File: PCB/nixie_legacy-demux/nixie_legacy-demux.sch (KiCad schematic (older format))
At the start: 38 parts, among them J1 HEADER_3, J2 K155ID1, Q1 MPSA42, Q2 MPSA42, Q3 MPSA42, Q4 MPSA42, Q5 MPSA42, Q6 MPSA42, U1 ATMEGA328P-PU, U2 MC7805CT-BP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

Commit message: added i2c_rtc_test.c to test interfacing with RX8025 rtc module
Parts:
- added J4: RX-8025SA, Package_SO:SOP-16_4.4x10.4mm_P1.27mm, symbol w_connectors:HEADER_14
- added R20, R21: 3.3k, Resistor_THT:R_Axial_DIN0207_L6.3mm_D2.5mm_P7.62mm_Horizontal, symbol Device:R_US
- gave numbers to parts that had none: 4
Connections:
- wire segments 175 -> 201
- no-connect marks 13 -> 22
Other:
- note added: "should I add a backup battery???"
- note removed: "If we add a clock module,\nthis is where it can go.\n\nIt will need to slot into the control board \nusing some sort of breakout header, probably. \n\nCommunication is over I2C, I think."

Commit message: Demux circuit schematic now complete with RTC (including 1Hz interrupt pin)
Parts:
- removed C1: 220nTANT, Capacitor_THT:C_Disc_D3.8mm_W2.6mm_P2.50mm, symbol Device:CP1
- removed SW1: Select_butt, symbol Switch:SW_Push
- removed SW2: Up_butt, symbol Switch:SW_Push
- removed SW3: Down_butt, symbol Switch:SW_Push
- removed U2: MC7805CT-BP, digikey-footprints:TO-220-3, symbol dk_PMIC-Voltage-Regulators-Linear:MC7805CT-BP
- added J5: HEADER_4, Connector_PinHeader_2.54mm:PinHeader_1x04_P2.54mm_Vertical, symbol w_connectors:HEADER_4
- J3: footprint (none) -> Connector_PinHeader_2.54mm:PinHeader_2x09_P2.54mm_Vertical
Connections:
- net labels removed: 9v
- wire segments 201 -> 194
- no-connect marks 22 -> 19
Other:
- note added: "down\nup\nselect\nGND"
- note removed: "should I add a backup battery???"
- moved on the sheet: J4, R20, R21

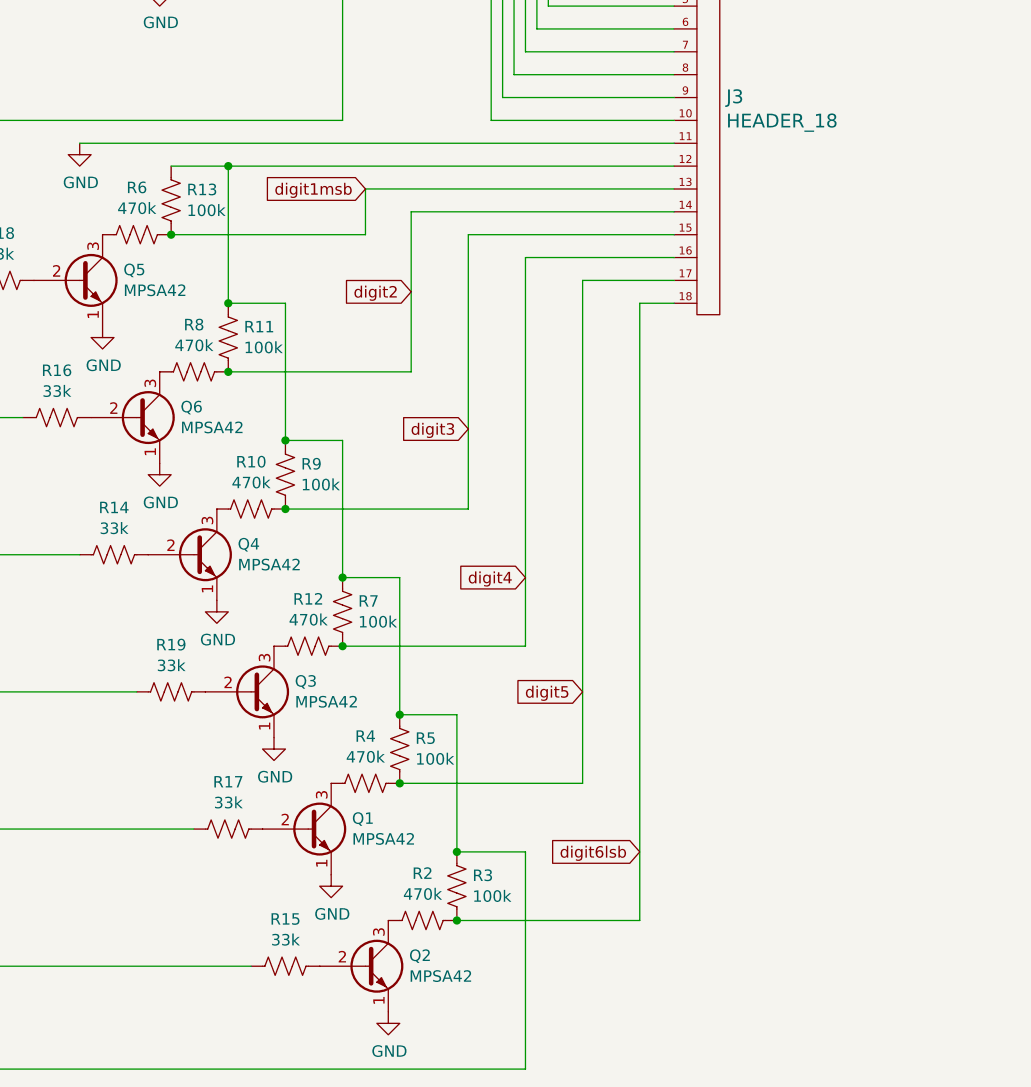
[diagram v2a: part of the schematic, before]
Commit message: Adding demux PCB v1: uses resistor network for 100k, has npn on board but pnp is on digit board
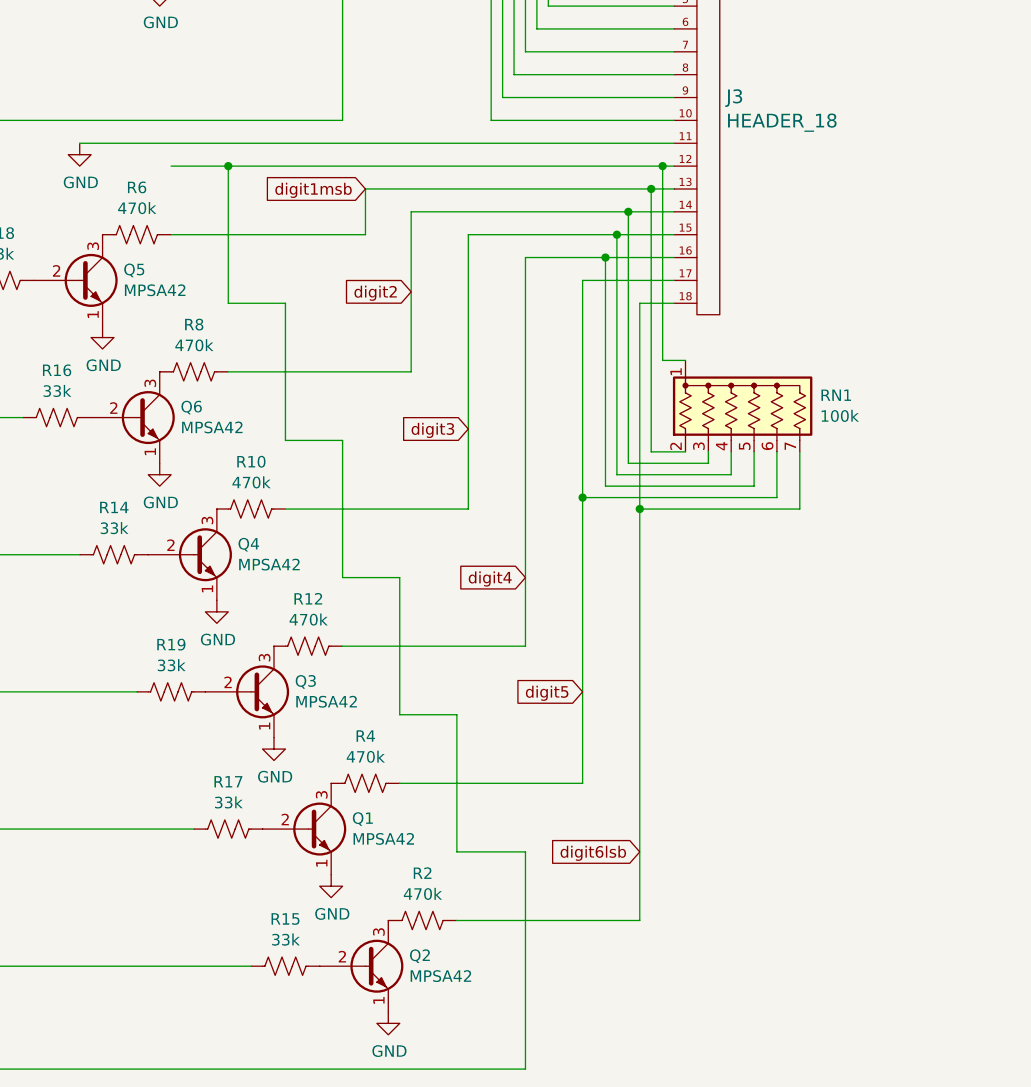
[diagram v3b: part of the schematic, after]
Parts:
- removed R11, R13, R3, R5, R7, R9: 100k, Resistor_THT:R_Axial_DIN0207_L6.3mm_D2.5mm_P7.62mm_Horizontal, symbol Device:R_US
- added RN1: 100k, Resistor_THT:R_Array_SIP7, symbol Device:R_Network06_US
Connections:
- net 200v: now also RN1.1 (common)
- net digit1msb: now also RN1.2 (R1)
- net digit2: now also RN1.3 (R2)
- net digit3: now also RN1.4 (R3)
- net digit4: now also RN1.5 (R4)
- net digit5: now also RN1.6 (R5)
- net digit6lsb: now also RN1.7 (R6)
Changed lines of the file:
@@
-$EndComp
-$Comp
-L Device:R_US R3
-U 1 1 60FDEAA9
-P 5900 6850
-F 0 "R3" H 5968 6896 50  0000 L CNN
-F 1 "100k" H 5968 6805 50  0000 L CNN
-F 2 "Resistor_THT:R_Axial_DIN0207_L6.3mm_D2.5mm_P7.62mm_Horizontal" V 5940 6840 50  0001 C CNN
-F 3 "~" H 5900 6850 50  0001 C CNN
-	1    5900 6850
-	1    0    0    -1
-$EndComp
-$Comp
-L Device:R_US R5
-U 1 1 60FDEAB3
-P 5650 6250
-F 0 "R5" H 5718 6296 50  0000 L CNN
-F 1 "100k" H 5718 6205 50  0000 L CNN
-F 2 "Resistor_THT:R_Axial_DIN0207_L6.3mm_D2.5mm_P7.62mm_Horizontal" V 5690 6240 50  0001 C CNN
-F 3 "~" H 5650 6250 50  0001 C CNN
-	1    5650 6250
-	1    0    0    -1
-$EndComp
-$Comp
-L Device:R_US R7
-U 1 1 60FDEABD
-P 5400 5650
-F 0 "R7" H 5468 5696 50  0000 L CNN
-F 1 "100k" H 5468 5605 50  0000 L CNN
-F 2 "Resistor_THT:R_Axial_DIN0207_L6.3mm_D2.5mm_P7.62mm_Horizontal" V 5440 5640 50  0001 C CNN
-F 3 "~" H 5400 5650 50  0001 C CNN
-	1    5400 5650
-	1    0    0    -1
-$EndComp
-$Comp
-L Device:R_US R9
-U 1 1 60FDEAC7
-P 5150 5050
-F 0 "R9" H 5218 5096 50  0000 L CNN
-F 1 "100k" H 5218 5005 50  0000 L CNN
-F 2 "Resistor_THT:R_Axial_DIN0207_L6.3mm_D2.5mm_P7.62mm_Horizontal" V 5190 5040 50  0001 C CNN
-F 3 "~" H 5150 5050 50  0001 C CNN
-	1    5150 5050
-	1    0    0    -1
-$EndComp
-$Comp
-L Device:R_US R11
-U 1 1 60FDEAD1
-P 4900 4450
-F 0 "R11" H 4968 4496 50  0000 L CNN
-F 1 "100k" H 4968 4405 50  0000 L CNN
-F 2 "Resistor_THT:R_Axial_DIN0207_L6.3mm_D2.5mm_P7.62mm_Horizontal" V 4940 4440 50  0001 C CNN
-F 3 "~" H 4900 4450 50  0001 C CNN
-	1    4900 4450
-	1    0    0    -1
 $EndComp
 $Comp
@@
 Wire Wire Line
 	5650 5500 5400 5500
-Connection ~ 5650 6100
 Wire Wire Line
 	5400 5500 5400 4900
 Wire Wire Line
 	5400 4900 5150 4900
-Connection ~ 5400 5500
 Wire Wire Line
 	5150 4900 5150 4300
 Wire Wire Line
 	5150 4300 4900 4300
-Connection ~ 5150 4900
 Wire Wire Line
 	4900 4300 4900 3700
 Wire Wire Line
 	4900 3700 4650 3700
-Connection ~ 4900 4300
 Wire Wire Line
 	1450 1150 1300 1150
@@
 Text GLabel 5950 4850 0    50   Input ~ 0
 digit3
-Connection ~ 5150 5200
-Connection ~ 5400 5800
-Connection ~ 5650 6400
-Connection ~ 5900 7000
-Connection ~ 4900 4600
 Text GLabel 5700 4250 0    50   Input ~ 0
 digit2
@@
 Wire Wire Line
 	1450 1700 1450 1150
-Connection ~ 5900 6700
 Wire Wire Line
 	2050 3800 3400 3800
@@
 	6850 4200 6450 4200
 Wire Wire Line
-	6850 4100 6200 4100
+	6850 4100 6550 4100
 Wire Wire Line
 	6200 4100 6200 5800
@@
 	5950 4000 5950 5200
 Wire Wire Line
-	6850 3900 5700 3900
-Wire Wire Line
 	5700 3900 5700 4600
 Wire Wire Line
 	5500 4000 5500 3800
 Wire Wire Line
-	5500 3800 6850 3800
+	5500 3800 6750 3800
 Wire Wire Line
 	4900 4600 5700 4600
@@
 $EndComp
 Wire Wire Line
-	6850 3700 4900 3700
+	6850 3700 6800 3700
 Connection ~ 4900 3700
 Wire Wire Line
@@
 	6850 3400 6100 3400
 Wire Wire Line
-	5950 4000 6850 4000
-Wire Wire Line
-	6450 4200 6450 6400
-Wire Wire Line
-	6700 4300 6700 7000
+	5950 4000 6600 4000
+Wire Wire Line
+	6450 4200 6450 5150
+Wire Wire Line
+	6700 4300 6700 5200
 Wire Wire Line
 	5400 750  5400 950
@@
 Wire Wire Line
 	4650 4000 5500 4000
-Connection ~ 4650 4000
-$Comp
-L Device:R_US R13
-U 1 1 60FDEADB
-P 4650 3850
-F 0 "R13" H 4718 3896 50  0000 L CNN
-F 1 "100k" H 4718 3805 50  0000 L CNN
-F 2 "Resistor_THT:R_Axial_DIN0207_L6.3mm_D2.5mm_P7.62mm_Horizontal" V 4690 3840 50  0001 C CNN
-F 3 "~" H 4650 3850 50  0001 C CNN
-	1    4650 3850
-	1    0    0    -1
-$EndComp
 $Comp
 L Device:R_US R6
@@
 Wire Wire Line
 	1000 950  2650 950
+Wire Wire Line
+	6800 4550 6800 3700
+Connection ~ 6800 3700
+Wire Wire Line
+	6800 3700 4900 3700
+Wire Wire Line
+	6750 4950 6750 3800
+Connection ~ 6750 3800
+Wire Wire Line
+	6750 3800 6850 3800
+Wire Wire Line
+	6850 3900 6650 3900
+Wire Wire Line
+	7000 4950 7000 5000
+Wire Wire Line
+	6650 5000 6650 3900
+Connection ~ 6650 3900
+Wire Wire Line
+	6650 3900 5700 3900
+Wire Wire Line
+	7100 4950 7100 5050
+Wire Wire Line
+	6600 5050 6600 4000
+Connection ~ 6600 4000
+Wire Wire Line
+	6600 4000 6850 4000
+Wire Wire Line
+	7200 4950 7200 5100
+Wire Wire Line
+	6550 5100 6550 4100
+Connection ~ 6550 4100
+Wire Wire Line
+	6550 4100 6200 4100
+Wire Wire Line
+	7300 4950 7300 5150
+Connection ~ 6450 5150
+Wire Wire Line
+	6450 5150 6450 6400
+Connection ~ 6700 5200
+Wire Wire Line
+	6700 5200 6700 7000
+$Comp
+L Device:R_Network06_US RN1
+U 1 1 611CFE58
+P 7200 4750
+F 0 "RN1" H 7488 4796 50  0000 L CNN
+F 1 "100k" H 7488 4705 50  0000 L CNN
+F 2 "Resistor_THT:R_Array_SIP7" V 7575 4750 50  0001 C CNN
+F 3 "http://www.vishay.com/docs/31509/csc.pdf" H 7200 4750 50  0001 C CNN
+	1    7200 4750
+	1    0    0    -1
+$EndComp
+Wire Wire Line
+	6900 4950 6750 4950
+Wire Wire Line
+	6900 4550 6800 4550
+Wire Wire Line
+	7000 5000 6650 5000
+Wire Wire Line
+	7100 5050 6600 5050
+Wire Wire Line
+	7200 5100 6550 5100
+Wire Wire Line
+	7300 5150 6450 5150
+Wire Wire Line
+	7400 5200 6700 5200
+Wire Wire Line
+	7400 4950 7400 5200
 $EndSCHEMATC

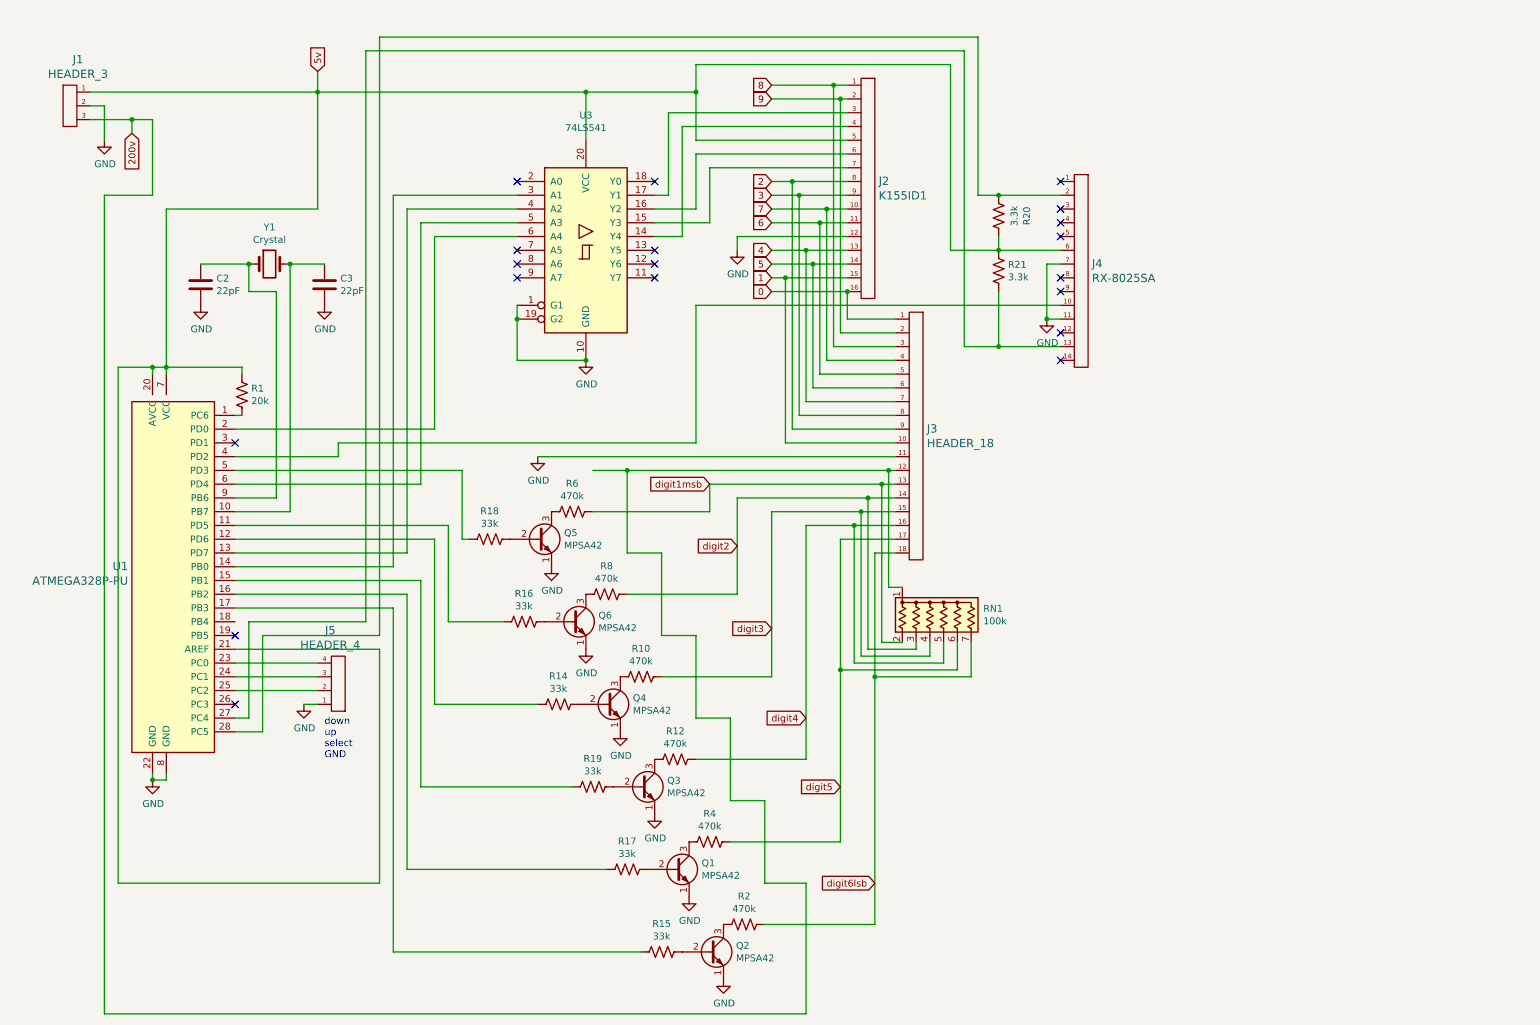
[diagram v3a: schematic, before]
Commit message: demux pcb v2, has MPSA92 transistors on this board instead of digit board, reducing connector to 16 pins instead of 18.
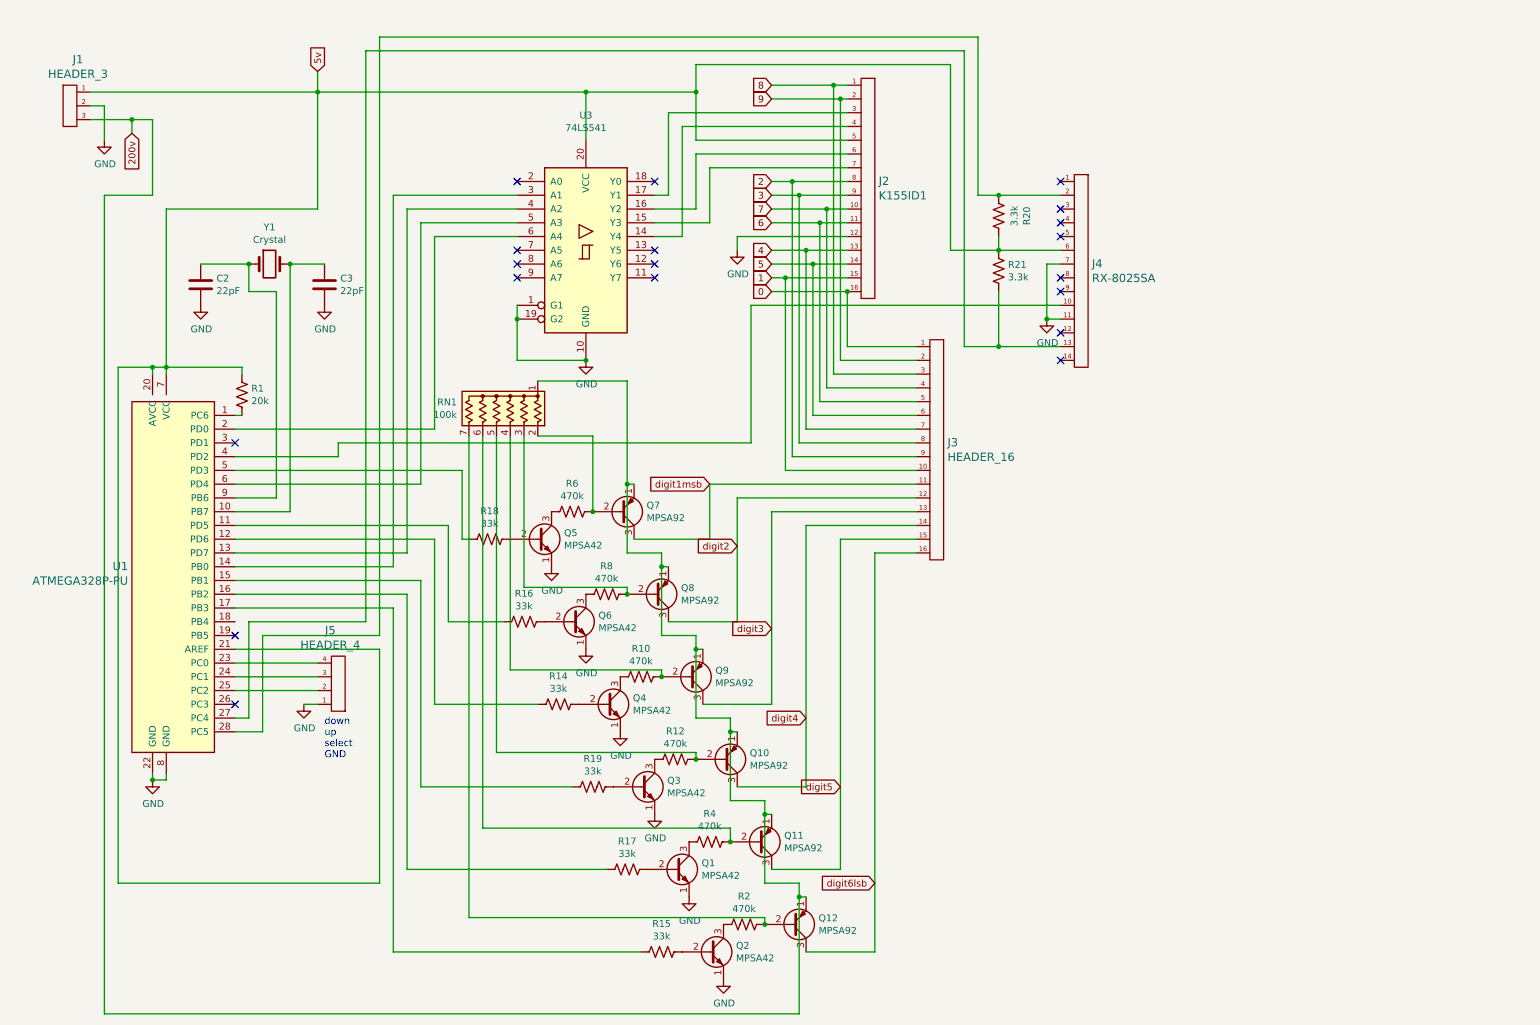
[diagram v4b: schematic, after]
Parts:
- removed J3: HEADER_18, Connector_PinHeader_2.54mm:PinHeader_2x09_P2.54mm_Vertical, symbol w_connectors:HEADER_18
- added J3: HEADER_16, Connector_PinSocket_2.54mm:PinSocket_2x08_P2.54mm_Vertical, symbol w_connectors:HEADER_16
- added Q10, Q11, Q12, Q7, Q8, Q9: MPSA92, Package_TO_SOT_THT:TO-92L_Inline_Wide, symbol Transistor_BJT:MPSA92
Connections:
- net 0: now also J3.1
- net 1: now also J3.10
- net 2: now also J3.9
- net 200v: now also Q10.1 (E), Q11.1 (E), Q12.1 (E), Q7.1 (E), Q8.1 (E), Q9.1 (E)
- net 3: now also J3.8
- net 4: now also J3.7
- net 5: now also J3.6
- net 6: now also J3.5
- net 7: now also J3.4
- net 8: now also J3.3
- net 9: now also J3.2
- net digit1msb: now also J3.11, Q7.3 (C); no longer R6.1, RN1.2 (R1)
- net digit2: now also J3.12, Q8.3 (C); no longer R8.1, RN1.3 (R2)
- net digit3: now also J3.13, Q9.3 (C); no longer R10.1, RN1.4 (R3)
- net digit4: now also J3.14, Q10.3 (C); no longer R12.1, RN1.5 (R4)
- net digit5: now also J3.15, Q11.3 (C); no longer R4.1, RN1.6 (R5)
- net digit6lsb: now also J3.16, Q12.3 (C); no longer R2.1, RN1.7 (R6)
- new net: Q12.2 (B), R2.1, RN1.7 (R6)
- new net: Q11.2 (B), R4.1, RN1.6 (R5)
- new net: Q7.2 (B), R6.1, RN1.2 (R1)
- new net: Q8.2 (B), R8.1, RN1.3 (R2)
- new net: Q9.2 (B), R10.1, RN1.4 (R3)
- new net: Q10.2 (B), R12.1, RN1.5 (R4)
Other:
- moved on the sheet: RN1

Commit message: demux pcb update: footprint for rtc was sop 16 instead of sop 14. rerouted power traces. shortened to 3.75"
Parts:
- added JP1: Decimal Point, customPartsLibrary:Single_pad-1x1, symbol customPartsLibrary:Single_pad
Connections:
- net at U1.19 (PB5): now also U3.7 (A5)
- net at U3.13 (Y5): now also JP1.1
- no-connect marks 19 -> 16
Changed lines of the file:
@@
 NoConn ~ 4100 2300
 NoConn ~ 4100 2200
-NoConn ~ 4100 2100
 NoConn ~ 4100 1600
 NoConn ~ 5100 1600
 NoConn ~ 5100 2300
 NoConn ~ 5100 2200
-NoConn ~ 5100 2100
 $Comp
 L w_connectors:HEADER_16 J2
@@
 Wire Wire Line
 	2050 5000 3100 5000
-NoConn ~ 2050 4900
 NoConn ~ 2050 5400
 Wire Wire Line
@@
 Wire Wire Line
 	4250 3450 4650 3450
+Wire Wire Line
+	2050 4900 2100 4900
+Wire Wire Line
+	2100 4900 2100 4850
+Wire Wire Line
+	2100 4850 2550 4850
+Wire Wire Line
+	2550 4850 2550 2900
+Wire Wire Line
+	2550 2900 3900 2900
+Wire Wire Line
+	3900 2900 3900 2100
+Wire Wire Line
+	3900 2100 4100 2100
+$Comp
+L customPartsLibrary:Single_pad JP1
+U 1 1 61148ED5
+P 5200 2100
+F 0 "JP1" H 5328 2151 50  0000 L CNN
+F 1 "Decimal Point" H 5328 2060 50  0000 L CNN
+F 2 "customPartsLibrary:Single_pad-1x1" H 4650 1650 50  0001 C CNN
+F 3 "" H 4650 1650 50  0001 C CNN
+	1    5200 2100
+	1    0    0    -1
+$EndComp
 $EndSCHEMATC
